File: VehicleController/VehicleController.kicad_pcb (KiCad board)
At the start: 4 copper layers, 127 x 68.6 mm, 143 parts, among them J1 CONN_02X06, J10 CONN_01X12, J2 USF_SLAVE_I2C, J5 I2C_0, J6 I2C_1, J7 CAN_SER, J8 CONN_01X03, J9 CONN_01X12, P1 OUTPUTS, P2 OUTPUTS, P4 CONN_01X02, P5 CONN_02X04, Q1 Q_NMOS_GSD, Q2 Q_NMOS_GSD, Q3 Q_NMOS_GSD, Q4 Q_PMOS_GSD, Q5 Q_NMOS_GSD, Q6 Q_NMOS_GSD, Q7 Q_NMOS_GSD, U1 BTS4130QGA, U10 BTS6133D, U11 R-78E5.0-1.0, U12 FGMMOPA6H, U13 U.FL_Antenna, U14 NDC7002N, U15 MCP2551, U16 MC_Override, U17 MCR_Shtdwn, U18 MCL_Shtdwn, U19 RI-0505S, U2 BTS4130QGA, U20 ISO1540, U21 TCMT1103, U22 OPTO-TRANSISTOR-4, U23 PC_RLY, U24 MCP47FEBX2, U3 BTS6133D, U4 BTS6133D, U5 H3LIS331DL, U6 UltimateSensorFusion, U7 Teensy_3.5, U8 NDC7003P, U9 TL431

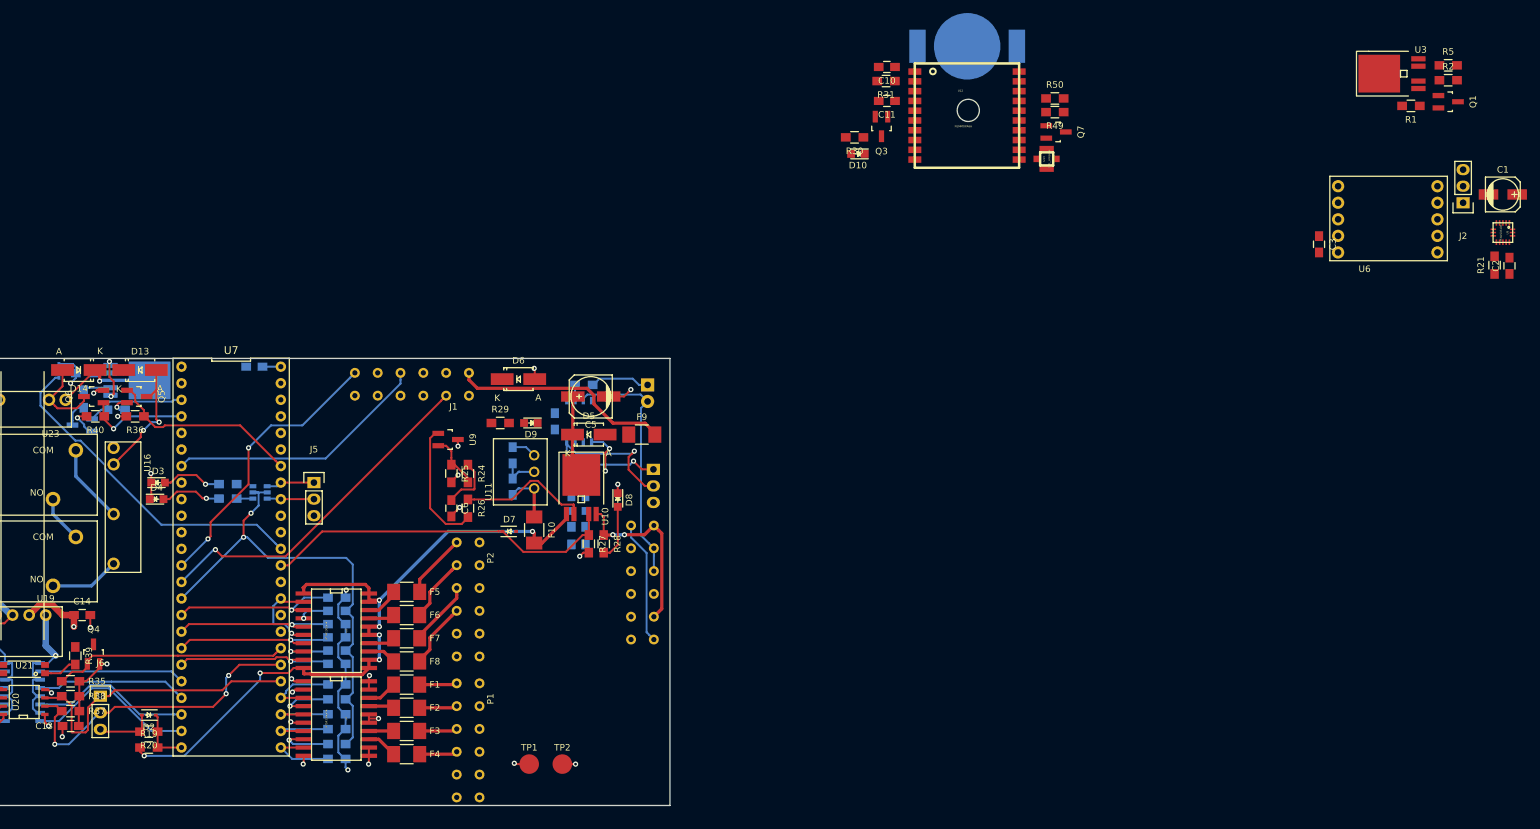
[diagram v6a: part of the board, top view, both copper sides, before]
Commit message: More VCU layout work
connectors changed to 2x4 molex nanofits for the 12v and 5v outputs.
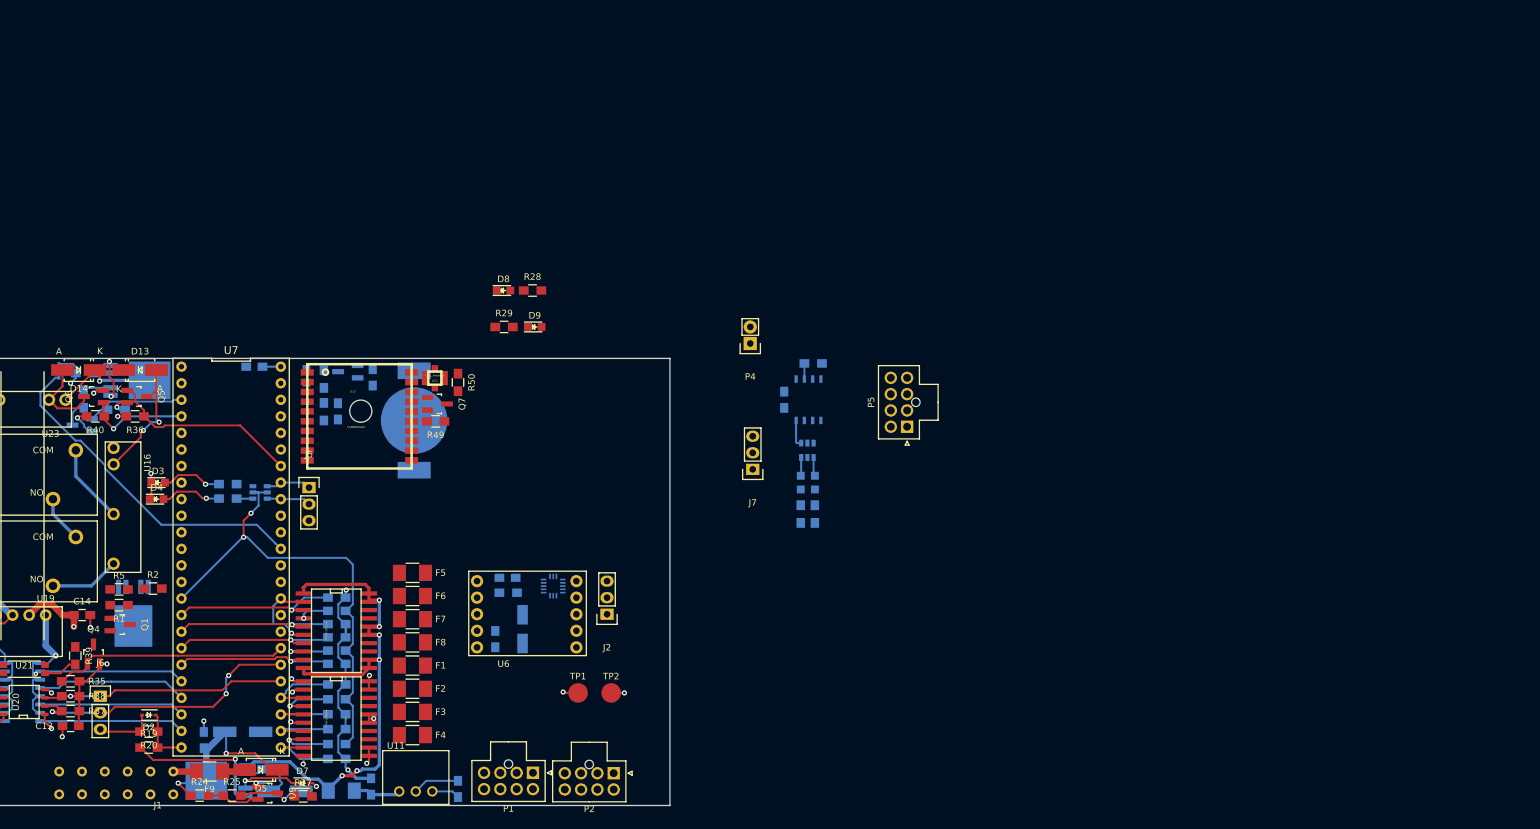
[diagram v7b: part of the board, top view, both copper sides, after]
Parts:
- C1, C10, C11, C2, C3, C5, C6, D10, D6, F10, Q3, R21, R26, R30, R31, U10, U3, U5: moved to B.Cu
- J7, P4: moved to F.Cu
- P1, P2: footprint UNCAMotorsports:MX120G-12 -> Connectors_Molex:Molex_NanoFit_2x04x2.50mm_Straight
- P5: footprint UNCAMotorsports:MX120G-12 -> Connectors_Molex:Molex_NanoFit_2x04x2.50mm_Straight; moved to F.Cu
- moved R5 219.2 mm to (55.2, 114.2)
- moved Q1 218.9 mm to (55.3, 119.6)
- moved R2 213.4 mm to (60.4, 114.0)
- moved R1 212.4 mm to (55.2, 116.6)
- moved U3 209.1 mm to (57.4, 119.8), turned to 0 degrees
- moved C1 164.5 mm to (117.1, 120.3), turned to 90 degrees
- moved C2 161.0 mm to (114.8, 112.4), turned to 0 degrees
- moved R21 159.4 mm to (114.9, 114.7), turned to 0 degrees
- moved U5 155.4 mm to (121.8, 113.7), turned to 180 degrees
- moved J2 145.7 mm to (130.0, 118.0)
- moved U6 145.3 mm to (118.1, 118.1)
- moved C3 140.1 mm to (112.9, 121.8)
- moved R49 106.2 mm to (103.8, 88.4)
- moved U12 104.0 mm to (92.1, 87.6)
- moved Q7 103.7 mm to (104.0, 85.7)
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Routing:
- net /AMS_F_OUT: track 53.3 -> 0.00 mm, vias 1 -> 0
- net /GLV_CURRENT: track 55.0 -> 11.4 mm, vias 0 -> 1
- net /IMD_F_OUT: track 43.4 -> 0.00 mm, vias 2 -> 0
- net /BRAKE_IN: track 40.5 -> 0.00 mm
- net /CAN Bus/CANH: track 38.1 -> 0.32 mm
- net +12V: track 138.4 -> 106.3 mm, vias 9 -> 7
- net +BATT: track 34.0 -> 3.57 mm
- net /CANTX: track 19.3 -> 0.00 mm, vias 3 -> 0
- net /CANRX: track 23.7 -> 4.49 mm, vias 1 -> 0
- net Net-(R26-Pad1): track 21.8 -> 2.82 mm
- net /CAN Bus/CANL: track 21.4 -> 2.41 mm
- net Net-(D6-Pad1): track 19.6 -> 8.92 mm, vias 0 -> 1
- net Net-(F7-Pad1): track 10.1 -> 0.00 mm
- net Net-(F5-Pad1): track 9.95 -> 0.00 mm
- net Net-(F8-Pad1): track 10.1 -> 0.25 mm
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
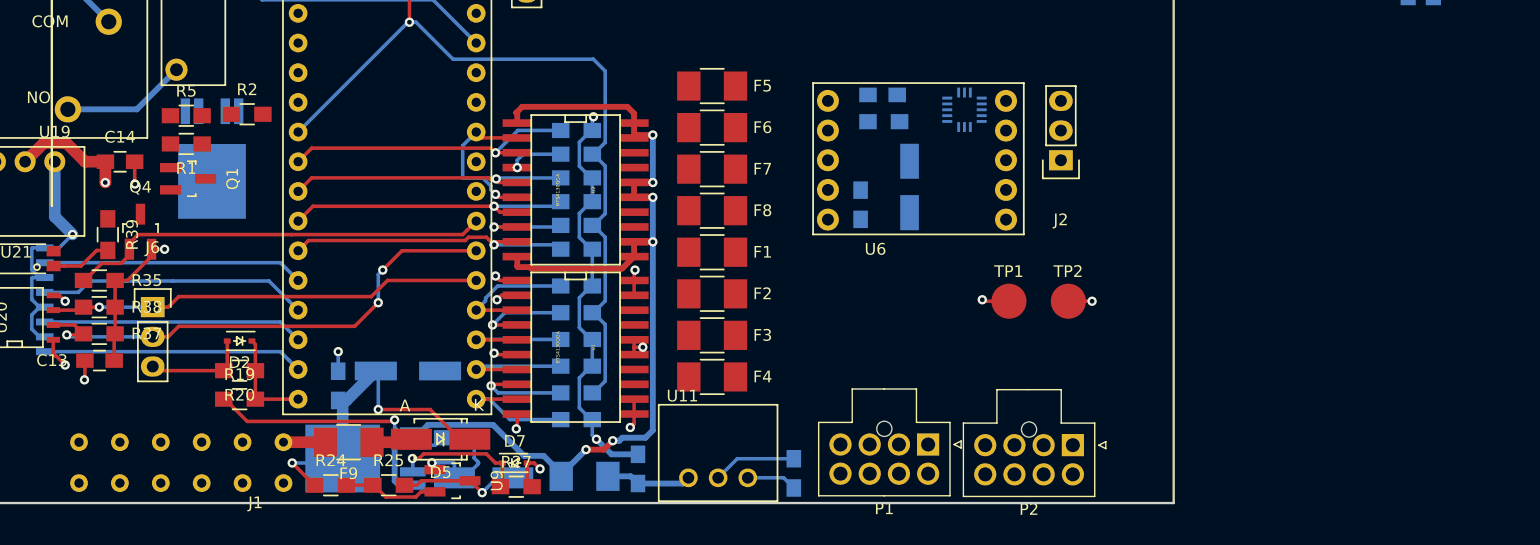
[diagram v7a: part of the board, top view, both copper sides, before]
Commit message: 2x10 connector is now a nanofit, VCU
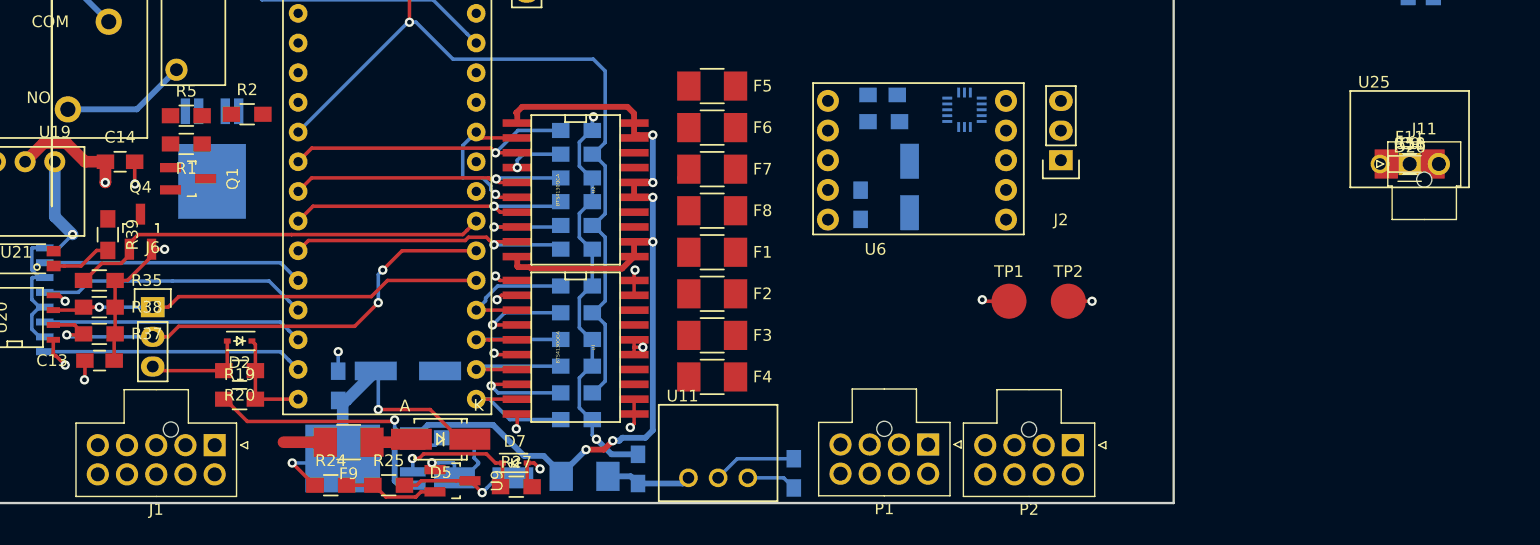
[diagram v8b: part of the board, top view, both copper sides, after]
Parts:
- added C18: 22u, Capacitors_SMD:C_0805_HandSoldering, F.Cu at (159.9, 118.3)
- added C9: 10u, Capacitors_SMD:C_0805_HandSoldering, F.Cu at (159.9, 118.3)
- added D20: RPI_PWR, LEDs:LED_0805, F.Cu at (159.9, 118.3)
- added F11: 2A, Resistors_SMD:R_1210_HandSoldering, F.Cu at (159.9, 118.3)
- added J11: RPI_PWR, Connectors_Molex:Molex_NanoFit_1x02x2.50mm_Straight, F.Cu at (159.9, 118.3)
- added R51: 470, Resistors_SMD:R_0805_HandSoldering, F.Cu at (159.9, 118.3)
- added U25: V7805W-2000, UNCAMotorsports:R-78Cxx-1.0, F.Cu at (159.9, 118.3)
- J1: value CONN_02X06 -> CONN_02X05; footprint UNCAMotorsports:MX120G-12 -> Connectors_Molex:Molex_NanoFit_2x05x2.50mm_Straight
- moved J1 5.90 mm to (57.6, 142.4)
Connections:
- J1 pad 10: (no net) -> GND
